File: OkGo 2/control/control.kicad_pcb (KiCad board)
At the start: 2 copper layers, 90.5 x 51 mm, 63 parts, among them P102 KEYSW, P103 BATT_CASE, P105 BATT, P106 ARM_LED, P108 SMA, P110 POWER_SW, P201 CH1, P202 CH2, P205 CH3, P206 CH4, Q201 BSS138BK, Q202 BSS138BK, Q203 BSS138BK, Q204 BSS138BK, U101 SWD, U102 STM32F071CBT6, U103 MEJ2S0305SC, U105 RFM95W, U106 LCD_HD44780, U107 ADP3335, Y101 8MHz

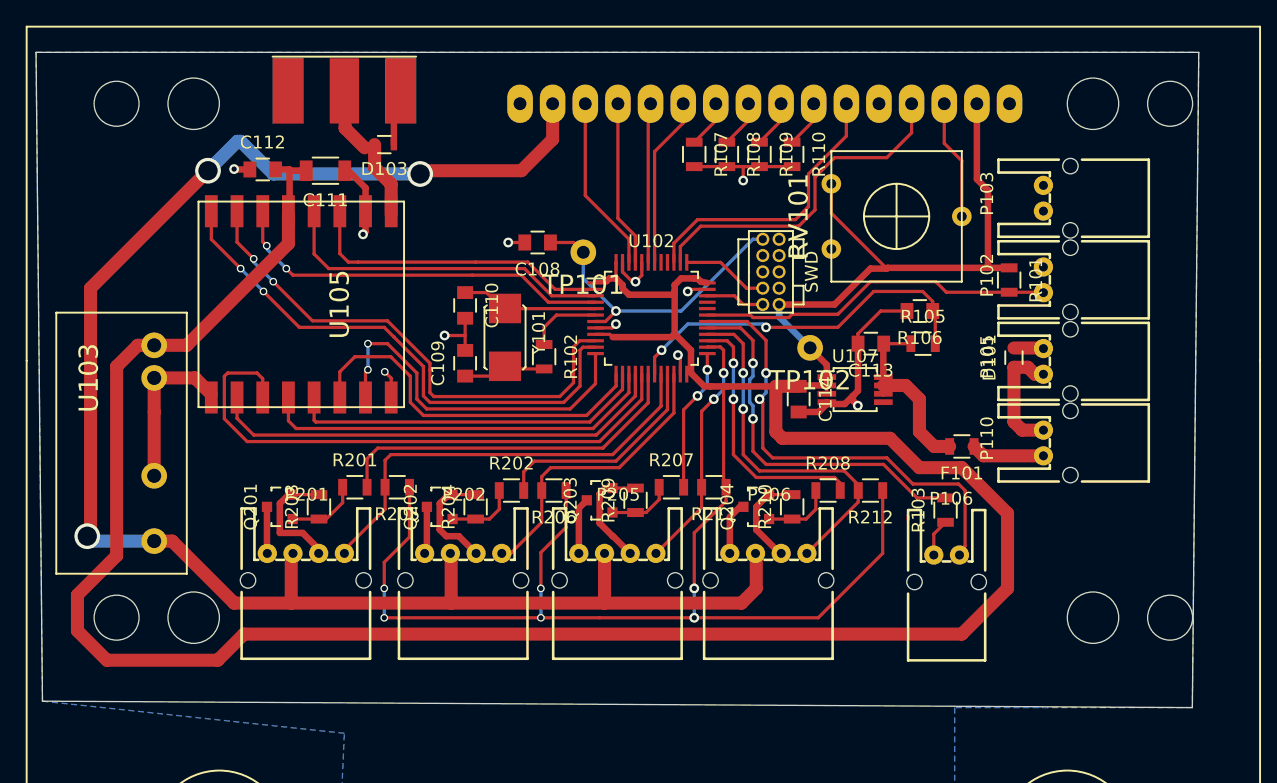
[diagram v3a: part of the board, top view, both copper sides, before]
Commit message: Added serial interface, resolves #19
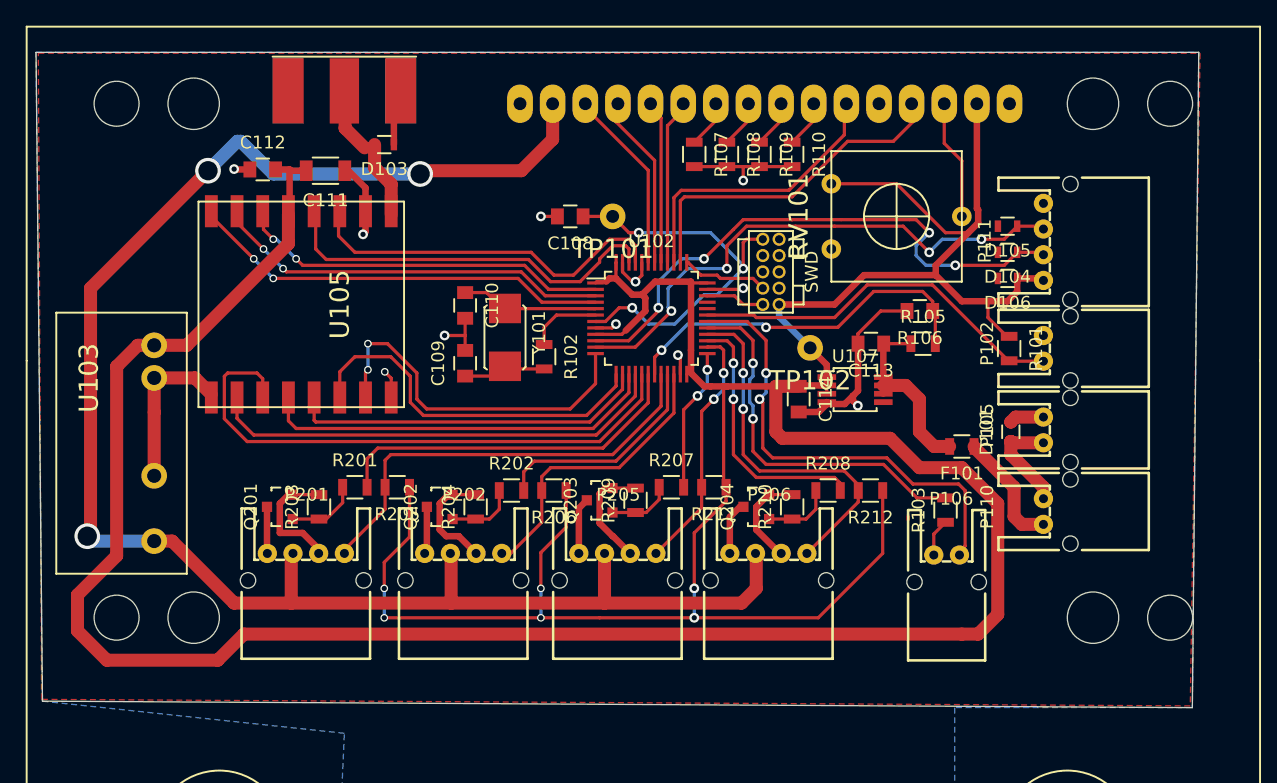
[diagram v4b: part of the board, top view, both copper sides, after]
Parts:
- removed P103: BATT_CASE, common:JST-PA-2
- added D104: TVS_small, Resistors_SMD:R_0603, F.Cu at (102.6, 51.6)
- added D105: TVS_small, Resistors_SMD:R_0603, F.Cu at (102.6, 49.5)
- added D106: TVS_small, Resistors_SMD:R_0603, F.Cu at (102.6, 53.6)
- added P111: SERIAL, common:JST-PA-4, F.Cu at (105.4, 47.8)
- moved D101 5.78 mm to (102.9, 65.5)
- moved P102 5.33 mm to (105.4, 58.0)
- moved P110 5.33 mm to (105.4, 70.7)
- moved R101 5.33 mm to (102.7, 59.1)
- moved P105 5.33 mm to (105.4, 64.4)
- moved TP101 3.61 mm to (71.9, 48.8)
- moved C108 3.25 mm to (68.6, 48.8)
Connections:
- U101 pad 6: Net-(U101-Pad6) -> (no net)
- U101 pad 7: Net-(U101-Pad7) -> (no net)
- U101 pad 8: Net-(U101-Pad8) -> (no net)
- U102 pad 10: /RFM_DIO1 -> Net-(D104-Pad1)
- U102 pad 11: /RFM_DIO2 -> Net-(D105-Pad1)
- U102 pad 2: /RFM_DIO3 -> /RFM_DIO0
- U102 pad 3: /RFM_DIO4 -> /RFM_DIO1
- U102 pad 32: Net-(U102-Pad32) -> (no net)
- U102 pad 33: Net-(U102-Pad33) -> (no net)
- U102 pad 4: /RFM_DIO0 -> /RFM_DIO2
- U102 pad 40: Net-(U102-Pad40) -> /LCD_DB4
- U102 pad 41: Net-(U102-Pad41) -> /LCD_DB5
- U102 pad 42: /LCD_DB4 -> /LCD_DB6
- U102 pad 43: /LCD_DB5 -> /LCD_DB7
- U102 pad 45: /LCD_DB6 -> /RFM_DIO3
- U102 pad 46: /LCD_DB7 -> /RFM_DIO4
- U107 pad 5: Net-(U107-Pad5) -> (no net)
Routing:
- net Net-(D104-Pad1): track 0.00 -> 44.9 mm, vias 0 -> 4
- net Net-(D105-Pad1): track 0.00 -> 43.1 mm, vias 0 -> 4
- net +3V3: track 329.6 -> 342.9 mm
- net /RFM_DIO1: track 40.0 -> 31.1 mm
- net /RFM_DIO2: track 41.9 -> 33.5 mm
- net /nRST: track 24.5 -> 32.6 mm, vias 1 -> 3
- net /RFM_DIO3: track 24.1 -> 29.4 mm
- net /RFM_DIO4: track 26.3 -> 31.3 mm
- net Net-(F101-Pad1): track 5.70 -> 9.28 mm
- net /ARM_SW: track 27.8 -> 30.0 mm
- net GND: track 105.3 -> 107.0 mm
- net /LCD_DB6: track 12.9 -> 13.9 mm
- net Net-(D101-Pad1): track 9.33 -> 8.35 mm
- net /RFM_DIO0: track 30.1 -> 29.2 mm
- net /LCD_DB4: track 13.3 -> 14.0 mm
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- added copper zone on F.Cu, net GND

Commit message: Revised control board outline
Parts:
- removed REF**: Hammond_1553T, control:Hammond_1553T
- added M3_MOUNT: VAL**, common:M3_MOUNT, F.Cu at (137.9, 80.3)
- added M3_MOUNT: VAL**, common:M3_MOUNT, F.Cu at (137.9, 120.4)
- added M3_MOUNT: VAL**, common:M3_MOUNT, F.Cu at (219.7, 120.4)
- added M3_MOUNT: VAL**, common:M3_MOUNT, F.Cu at (219.7, 80.3)
- moved C109 354.1 mm to (411.8, 104.3), turned to 0 degrees
- moved C112 351.9 mm to (387.1, 126.5)
- moved R201 338.7 mm to (376.1, 167.7)
- moved Q201 336.0 mm to (369.7, 161.5), turned to 0 degrees
- moved R109 335.8 mm to (414.7, 98.0), turned to 0 degrees
- moved R102 335.4 mm to (395.9, 123.4), turned to 0 degrees
- moved Y101 335.2 mm to (394.3, 110.3), turned to 0 degrees
- moved R203 334.5 mm to (369.2, 168.0), turned to 0 degrees
- moved R110 333.6 mm to (412.8, 110.6), turned to 0 degrees
- moved C111 332.8 mm to (375.0, 114.7), turned to 0 degrees
- moved D103 332.7 mm to (376.5, 125.5), turned to 0 degrees
- moved C108 332.1 mm to (391.5, 126.5), turned to 0 degrees
- moved R202 331.9 mm to (385.2, 153.6)
- moved C110 330.7 mm to (382.1, 132.0), turned to 0 degrees
- moved R108 330.2 mm to (404.0, 111.6), turned to 0 degrees
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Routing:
- net +3V3: track 342.9 -> 0.00 mm, vias 6 -> 0
- net +5V: track 135.3 -> 0.00 mm, vias 3 -> 0
- net GND: track 107.0 -> 0.00 mm, vias 11 -> 0
- net Net-(D104-Pad1): track 44.9 -> 0.00 mm, vias 4 -> 0
- net /RFM_MOSI: track 44.3 -> 0.00 mm
- net Net-(D105-Pad1): track 43.1 -> 0.00 mm, vias 4 -> 0
- net /DISARM_LED: track 36.8 -> 0.00 mm, vias 2 -> 0
- net /RFM_MISO: track 36.4 -> 0.00 mm
- net /controls/CH1_SW: track 34.3 -> 0.00 mm
- net /RFM_DIO2: track 33.5 -> 0.00 mm, vias 2 -> 0
- net /nRST: track 32.6 -> 0.00 mm, vias 3 -> 0
- net /RFM_SCK: track 31.4 -> 0.00 mm
- net /RFM_DIO4: track 31.3 -> 0.00 mm
- net /RFM_DIO1: track 31.1 -> 0.00 mm, vias 2 -> 0
- net /ARM_SW: track 30.0 -> 0.00 mm
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- removed copper zone on B.Cu, net GND
- removed copper zone on F.Cu, net GND
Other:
- board size 90.5 x 51 mm -> 92.2 x 64.5 mm
- board text added: "ARM LED"
- board text added: "BATT"
- board text added: "CH1"
- board text added: "CH2"
- board text added: "CH3"
- board text added: "CH4"
- board text added: "KEY SW"
- board text added: "POW SW"
- board text added: "SERIAL"

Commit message: 2nd route of control, sans cleaning and checking
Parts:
- R106: footprint Capacitors_SMD:C_0805 -> Resistors_SMD:R_0805
- moved C109 259.4 mm to (152.4, 103.4), turned to 90 degrees
- moved C105 258.2 mm to (161.0, 106.7), turned to 270 degrees
- moved U101 248.6 mm to (137.4, 104.9), turned to 270 degrees
- moved C102 242.0 mm to (167.4, 96.0)
- moved C103 241.6 mm to (167.4, 94.0)
- moved C112 239.4 mm to (153.5, 73.8)
- moved Y101 238.9 mm to (155.7, 99.3), turned to 270 degrees
- moved TP101 238.3 mm to (138.7, 113.0)
- moved R102 237.7 mm to (159.0, 102.9), turned to 270 degrees
- moved C108 233.3 mm to (159.0, 106.7), turned to 270 degrees
- moved C110 232.1 mm to (152.4, 99.3), turned to 270 degrees
- moved C101 229.8 mm to (174.2, 110.2), turned to 270 degrees
- moved R201 227.5 mm to (154.2, 117.3), turned to 180 degrees
- moved C111 226.3 mm to (153.0, 70.9)
- moved R109 226.2 mm to (189.7, 74.9), turned to 90 degrees
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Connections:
- P111 pad 2: Net-(D105-Pad1) -> Net-(D104-Pad1)
- P111 pad 3: Net-(D104-Pad1) -> Net-(D105-Pad1)
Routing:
- net +3V3: track 0.00 -> 313.8 mm, vias 0 -> 1
- net +5V: track 0.00 -> 175.2 mm, vias 0 -> 1
- net GND: track 0.00 -> 119.3 mm, vias 0 -> 21
- net /BATT_MON: track 0.00 -> 65.9 mm, vias 0 -> 4
- net /ARM_SW: track 0.00 -> 57.6 mm, vias 0 -> 2
- net /SWDIO: track 0.00 -> 53.6 mm, vias 0 -> 2
- net /SWDCLK: track 0.00 -> 53.2 mm, vias 0 -> 2
- net Net-(D104-Pad1): track 0.00 -> 51.5 mm, vias 0 -> 2
- net /ARM_LED: track 0.00 -> 51.4 mm, vias 0 -> 2
- net /RFM_MOSI: track 0.00 -> 49.1 mm
- net /DISARM_LED: track 0.00 -> 47.8 mm, vias 0 -> 2
- net Net-(D105-Pad1): track 0.00 -> 47.7 mm, vias 0 -> 2
- net /RFM_SCK: track 0.00 -> 44.4 mm
- net /RFM_NSS: track 0.00 -> 44.3 mm
- net /RFM_RESET: track 0.00 -> 42.8 mm
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- added copper zone on B.Cu, net GND
- added copper zone on F.Cu, net GND

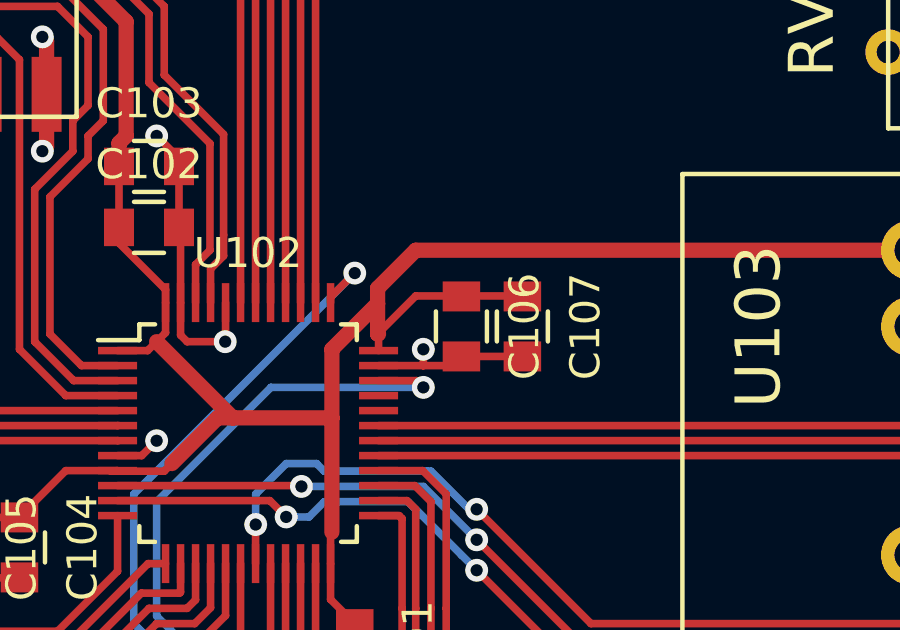
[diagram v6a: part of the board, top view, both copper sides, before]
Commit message: Provisional first place+pinassign+route of ignition
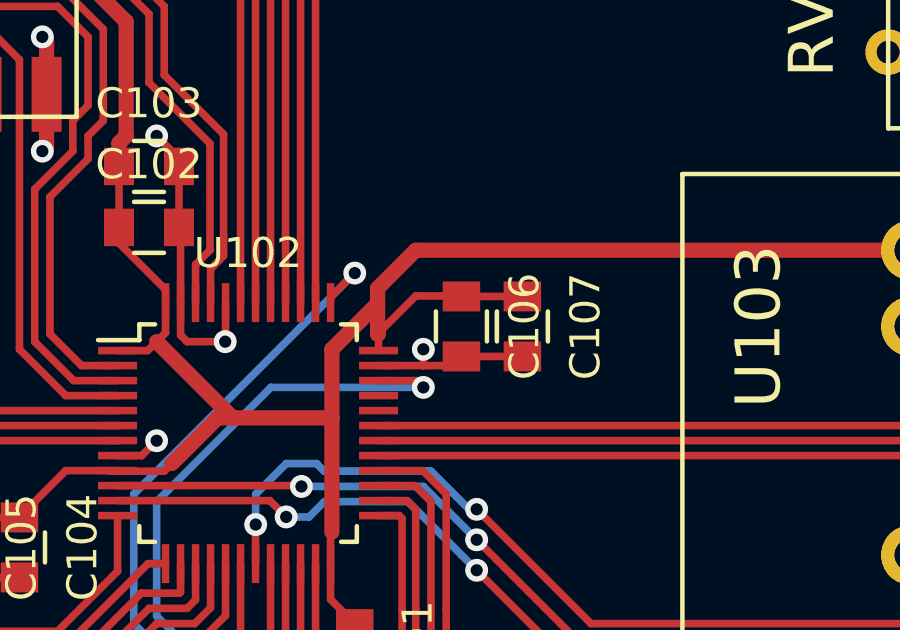
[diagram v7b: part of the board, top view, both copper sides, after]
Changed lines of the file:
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@@
   (general
     (links 172)
-    (no_connects 1)
+    (no_connects 0)
     (area 131.781381 64.915 227.315572 132.361)
     (thickness 1.6)
     (drawings 28)
-    (tracks 896)
+    (tracks 899)
     (zones 0)
     (modules 69)
@@
   )
   (setup
-    (last_trace_width 1.016)
+    (last_trace_width 0.25)
     (user_trace_width 0.254)
     (user_trace_width 0.508)
@@
   (gr_arc (start 216.916 71.374) (end 216.916 76.2) (angle 90) (layer Edge.Cuts) (width 0.1))
   (gr_arc (start 140.716 71.374) (end 145.542 71.374) (angle 90) (layer Edge.Cuts) (width 0.1))
+  (segment (start 175.006 99.568) (end 176.276 98.298) (width 0.254) (layer F.Cu) (net 1))
+  (segment (start 176.276 98.298) (end 177.8 98.298) (width 0.254) (layer F.Cu) (net 1))
+  (segment (start 177.8 98.298) (end 177.8 98.314) (width 0.254) (layer F.Cu) (net 1))
+  (segment (start 177.8 98.314) (end 179.816 98.314) (width 0.254) (layer F.Cu) (net 1))
+  (segment (start 179.816 98.314) (end 179.832 98.298) (width 0.254) (layer F.Cu) (net 1))
+  (segment (start 179.832 98.298) (end 179.832 98.314) (width 0.254) (layer F.Cu) (net 1))
   (segment (start 206.248 124.206) (end 206.248 120.396) (width 1.016) (layer F.Cu) (net 1))
   (segment (start 206.248 120.396) (end 206.248 117.094) (width 1.016) (layer F.Cu) (net 1))
@@
   (segment (start 192.532 96.774) (end 192.786 96.774) (width 0.254) (layer F.Cu) (net 1))
   (segment (start 175.038 100.12) (end 175.038 99.568) (width 0.254) (layer F.Cu) (net 1))
-  (segment (start 175.038 99.568) (end 175.038 99.536) (width 0.254) (layer F.Cu) (net 1))
-  (segment (start 175.038 99.536) (end 176.276 98.298) (width 0.254) (layer F.Cu) (net 1))
-  (segment (start 176.276 98.298) (end 179.832 98.298) (width 0.254) (layer F.Cu) (net 1))
   (segment (start 179.832 98.298) (end 179.832 98.314) (width 0.254) (layer F.Cu) (net 1))
   (segment (start 161.036 105.68) (end 163.052 105.68) (width 0.254) (layer F.Cu) (net 1))
